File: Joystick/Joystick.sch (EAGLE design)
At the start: 9 parts, among them U1 ATTINY48/88-TQFP, U2 JOYSTICK

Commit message: Check point of current PCB designs. Among other things I think this change includes rewiring of programming lines on many of the boards,.
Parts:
- removed U1: ATTINY48/88-TQFP, Modulo:ATTINY48/88-TQFP
- added R8, R9: 150Ω, Modulo:RESISTOR-150Ω
- added U3: ATTINY841, Modulo:ATTINY841
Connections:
- removed net LED: R1.2, U1.PB7
- removed net MISO: PCB1.MISO, U1.PB4
- removed net MOSI: PCB1.MOSI, U1.PB3
- removed net SCK: PCB1.SCK, U1.PB5
- new net MISO/LED: PCB1.MISO, R1.2, U3.PA5
- new net SCL/SCK: R8.2, U3.PA4
- new net SDA/MOSI: R9.2, U3.PA6
- net GND: now also U3.GND; no longer U1.GND, U1.GND@1
- net H: now also U3.PB1; no longer U1.PC0
- net RESET: now also U3.PB3; no longer U1.PC6
- net SCL: now also PCB1.SCK, R8.1; no longer U1.PC5
- net SDA: now also PCB1.MOSI, R9.1; no longer U1.PC4
- net SEL: now also U3.PB2; no longer U1.PC2
- net V: now also U3.PB0; no longer U1.PC1
- net VCC: now also U3.VCC; no longer U1.AVCC, U1.VCC

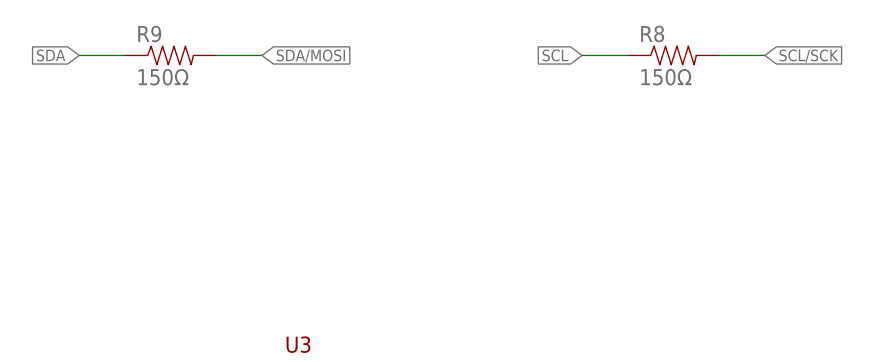
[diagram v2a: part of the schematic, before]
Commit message: Various small tweaks based on testing and feedback from manufacturer.
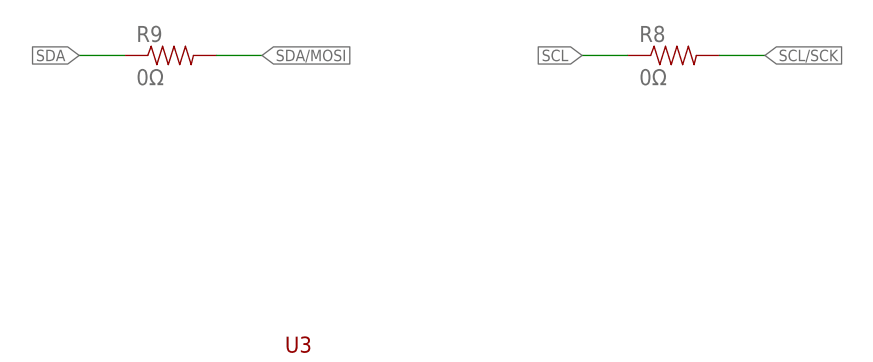
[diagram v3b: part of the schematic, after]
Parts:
- R8, R9: value 150Ω -> 0Ω; device Modulo:RESISTOR-150Ω -> Modulo:RESISTOR-0Ω
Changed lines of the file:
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@@
 </part>
 <part name="U3" library="Modulo" deviceset="ATTINY841" device=""/>
-<part name="R8" library="Modulo" deviceset="RESISTOR" device="-150Ω" value="150Ω"/>
-<part name="R9" library="Modulo" deviceset="RESISTOR" device="-150Ω" value="150Ω"/>
+<part name="R8" library="Modulo" deviceset="RESISTOR" device="-0Ω" value="0Ω"/>
+<part name="R9" library="Modulo" deviceset="RESISTOR" device="-0Ω" value="0Ω"/>
 </parts>
 <sheets>

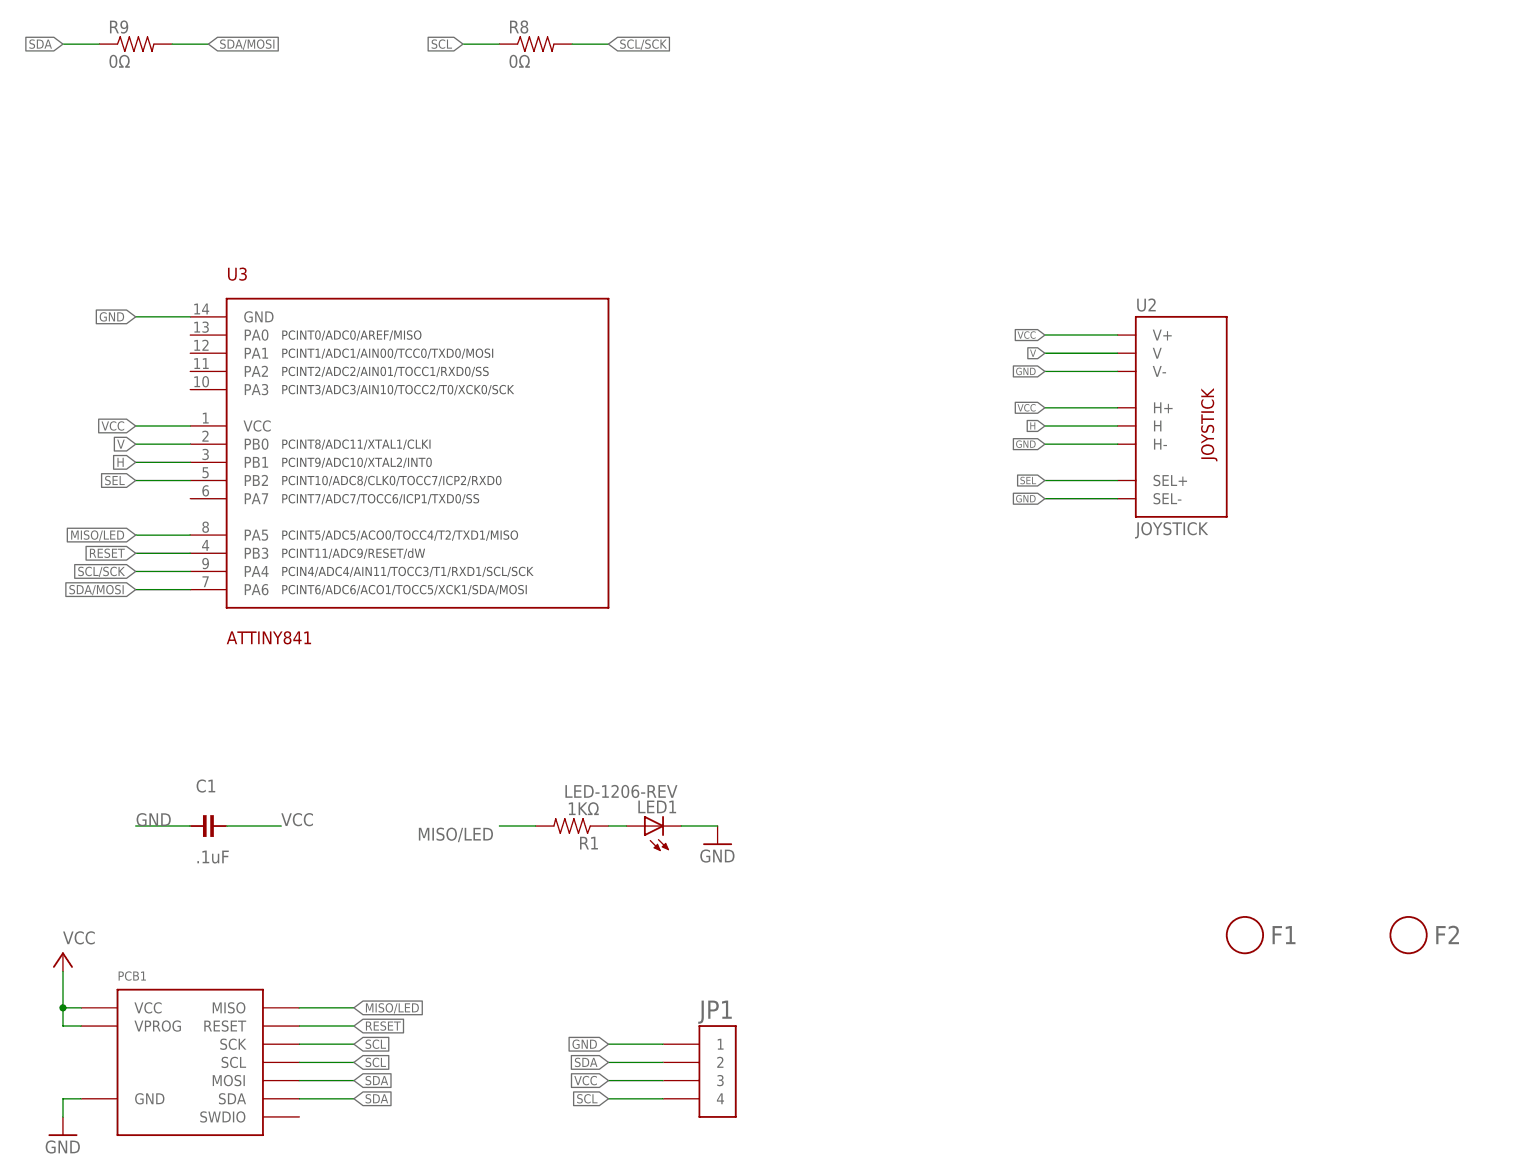
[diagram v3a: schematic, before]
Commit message: Added unique board prefixes to part numbers due to CM requirements
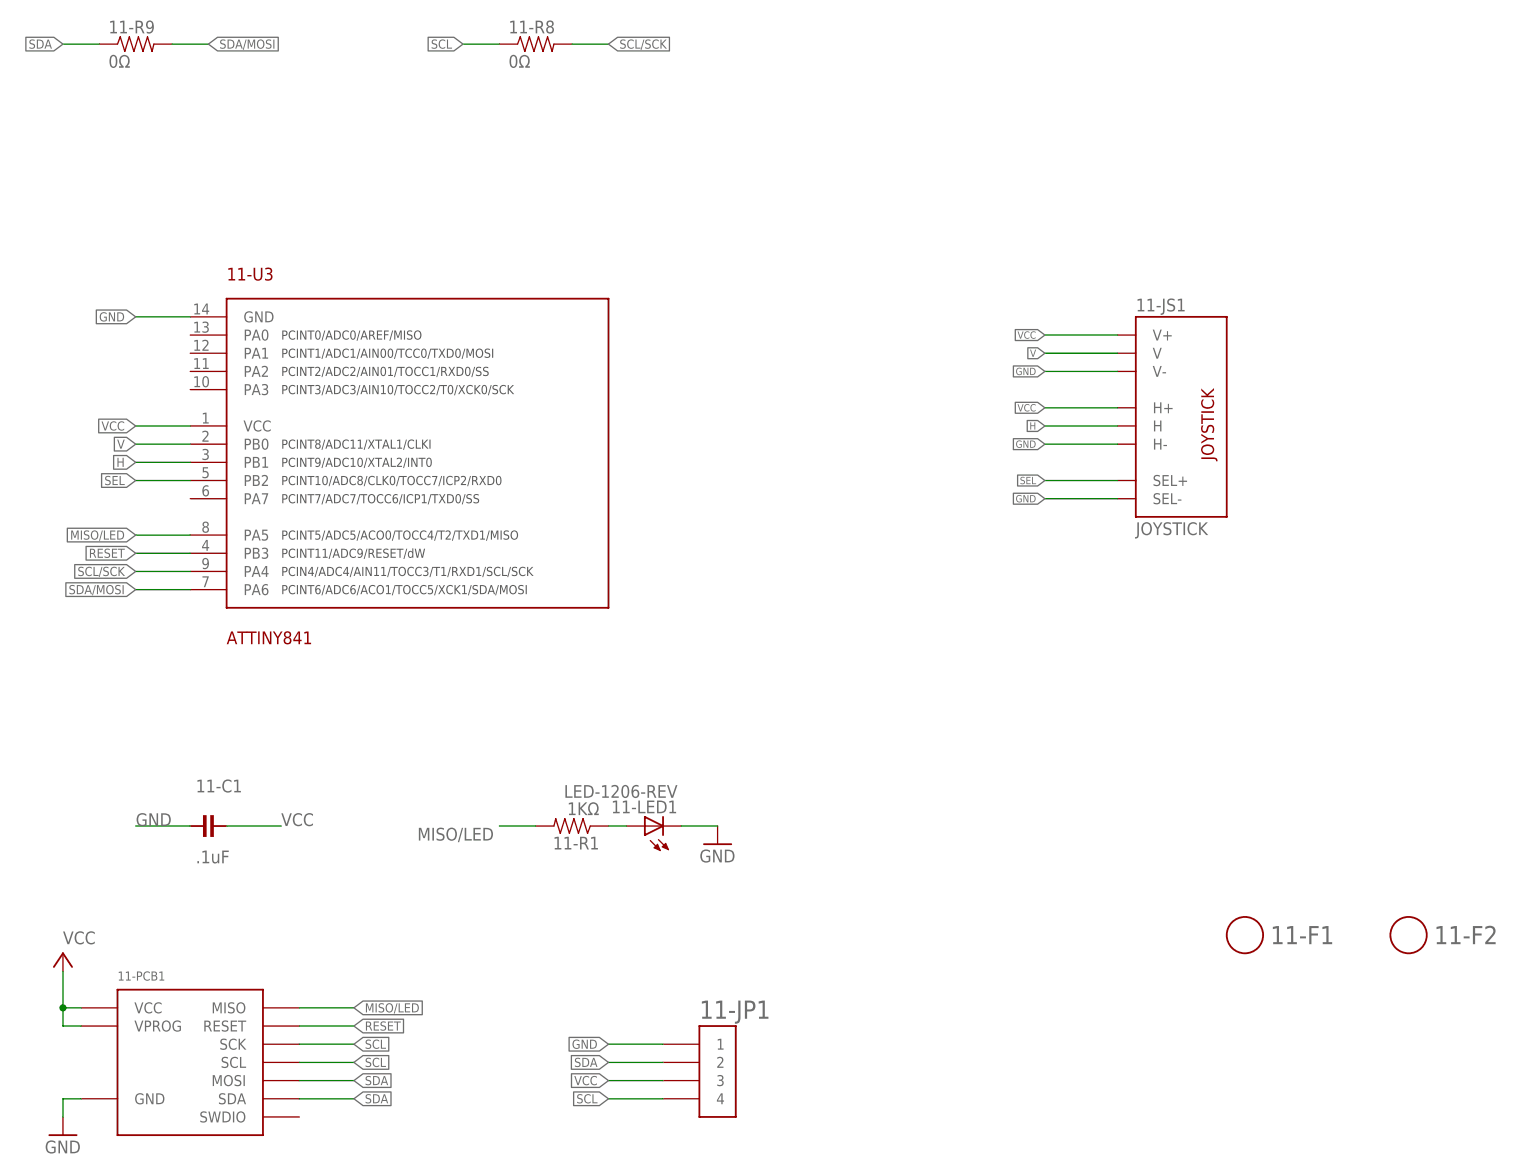
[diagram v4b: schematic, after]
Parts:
- renumbered C1 to 11-C1, F1 to 11-F1, F2 to 11-F2, JP1 to 11-JP1, LED1 to 11-LED1, PCB1 to 11-PCB1, R1 to 11-R1, R8 to 11-R8, R9 to 11-R9, U2 to 11-JS1, U3 to 11-U3
